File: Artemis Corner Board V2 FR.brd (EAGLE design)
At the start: 132.4 x 63.1 mm, 62 parts, among them U1 TPS562219, U10 TPS562219, U21 LM1085IS, U3 TPS562219, U4 MCP2562FD

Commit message: Everything done exept for scary LEDs
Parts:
- removed C21: 0.1uF, adafruit:C0805
- removed C24, C25, C26: 22uF, adafruit:C0805
- removed L3: 4.7uH, FormE:SRP6540
- removed LED7: GREEN, FormE:CHIPLED_0805
- removed R24: 5.76K, adafruit:R0805
- removed R25, R26: 10K, adafruit:R0805
- removed R27: 1K, adafruit:R0805
- removed U10: TPS562219, FormE:TPS562219
- C12: value 0.1uF -> 8200pF
- C13: value 10uF -> 0.1uF
- C14: value 10uF -> 22uF
- C15: value 8200pF -> 22uF
- C16: value 0.1uF -> 22uF
- C17, C19, C20: value 22uF -> 0.1uF; device adafruit:C0805 -> rcl:C0805
- C18: value 8200pF -> 0.1uF; device adafruit:C0805 -> rcl:C0805
- R5: value 26.1K -> 33.2K
- moved H1 155.9 mm to (9.17, 1.43)
- moved LED1 129.6 mm to (-56.5, 27.3)
- moved R8 97.1 mm to (53.3, 13.3)
- moved R9 97.1 mm to (60.3, -6.35)
- moved C11 96.7 mm to (64.1, 8.89)
- moved U3 96.7 mm to (53.3, 8.89)
- moved C10 96.7 mm to (61.6, 8.89)
- moved C9 96.7 mm to (59.1, 8.89)
- moved R5 96.7 mm to (47.6, 10.8)
- moved R6 96.7 mm to (47.6, 6.35)
- moved C16 83.9 mm to (57.8, 1.27), turned to 0 degrees
- moved L2 83.3 mm to (50.8, -1.91)
- moved LED3 83.0 mm to (55.9, -6.35)
- moved C12 82.2 mm to (50.2, 12.7), turned to 90 degrees
- moved C15 75.7 mm to (57.8, -1.27), turned to 0 degrees
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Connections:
- removed net +1V2: C17.1, C19.1, C20.1, C23.1, L2.P$2, LED3.A, R24.2, U2.11, U2.2, U2.26, U2.42, U2.54, U4.5
- removed net +2V8: C24.1, C25.1, C26.1, L3.P$2, LED7.A, R5.2
- removed net N$1001: R26.2, U10.7
- removed net N$28: LED3.C, R27.2
- removed net SS_5V: C15.1, U10.5
- removed net SW_5V: C16.2, L2.P$1, U10.2
- removed net VBST_5V: C16.1, U10.8
- removed net VFB_5V: R24.1, R25.2, U10.6
- new net IR_SENSOR_1_ANALOG_OUT: H1.28, U2.61
- new net IR_SENSOR_1_DIGITAL_IN: H1.12, U2.45
- new net IR_SENSOR_1_DIGITAL_OUT: H1.15, U2.49
- new net IR_SENSOR_2_ANALOG_OUT: H1.27, U2.62
- new net IR_SENSOR_2_DIGITAL_IN: H1.11, U2.50
- new net IR_SENSOR_2_DIGITAL_OUT: H1.14, U2.48
- new net IR_SENSOR_3_ANALOG_OUT: H1.26, U2.63
- new net IR_SENSOR_3_DIGITAL_IN: H1.10, U2.51
- new net IR_SENSOR_3_DIGITAL_OUT: H1.13, U2.47
- net +12V: now also H1.2, H1.3, H1.4, H1.5, H1.6; no longer H1.21, H1.28
- net +3V3: now also C17.1, C18.1, C19.1, C20.1, C23.1, U2.11, U2.2, U2.26, U2.42, U2.54, U4.5; no longer H1.7, H1.8
- net +5V: now also C14.1, C15.1, C16.1, L2.P$2, LED3.A, R5.2
- net DAMPER_POS_OUT: now also H1.25; no longer H1.35
- net GND: now also C16.2, H1.17, H1.18, H1.19, H1.20; no longer C13.2, C24.2, C25.2, C26.2, H1.2, H1.3, H1.4, H1.5, H1.6, R25.1, R27.1, U10.1
- net N$3: now also LED3.C; no longer LED7.C
- net PROGRAMMING_CAN_N: now also H1.35; no longer H1.34
- net PROGRAMMING_CAN_P: now also H1.34; no longer H1.33
- net SS_5V2: now also C12.1; no longer C18.1
- net STRAIN_GADGE_VOLTMETER_IN_0: no longer U2.8
- net STRAIN_GAUGE_VOLTMETER_OUT: no longer U2.28
- net SW_5V2: now also C13.2, L2.P$1; no longer C21.2, L3.P$1
- net VBST_5V2: now also C13.1; no longer C21.1
- net VCC: no longer C12.1, C13.1, C14.1, R26.1, U10.3
- net WHEEL_SPEED_OUT: now also H1.24; no longer H1.22
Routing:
- net PROGRAMMING_CAN_RX: track 17.2 -> 36.4 mm
- net +3V3: track 1.54 -> 19.8 mm, vias 6 -> 11
- net PROGRAMMING_CAN_TX: track 11.3 -> 26.1 mm
- net +1V2: track 11.0 -> 0.00 mm, vias 4 -> 0
- net N$1001: track 7.73 -> 0.00 mm, vias 2 -> 0
- net VFB_5V: track 6.85 -> 0.00 mm
- net N$11: track 0.00 -> 3.66 mm
- net VBST_5V: track 3.07 -> 0.00 mm
- net SS_5V: track 2.66 -> 0.00 mm
- net +5V: track 3.04 -> 5.48 mm, vias 7 -> 8
- net VCC: track 8.44 -> 6.05 mm, vias 24 -> 18
- net N$28: track 1.76 -> 0.00 mm
- net SW_5V2: track 1.75 -> 0.00 mm, vias 6 -> 8
- net +2V8: track 1.54 -> 0.00 mm, vias 6 -> 0
- net +12V: track 0.00 -> 1.49 mm, vias 7 -> 11
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- added copper zone on layer 15, net +3V3
- added copper zone on layer 15, net +5V
- added copper zone on layer 15, net N$5
- removed copper zone on layer 1, net +2V8
- removed copper zone on layer 1, net SW_5V
- removed copper zone on layer 16, net SW_5V

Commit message: Done  (1st)
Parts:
- added C21: 0.1uF, rcl:C0805
- added LED10, LED11, LED12, LED13, LED14, LED15, LED16, LED17, LED18, LED7, LED8, LED9: APA102C, FormE:5050_LED
- U2: value (none) -> TM4C1231C3PM
- moved LED4 102.7 mm to (29.8, -36.8)
- moved C20 87.8 mm to (8.89, -16.5)
- moved LED2 85.8 mm to (29.8, -22.9), turned to 270 degrees
- moved LED1 80.7 mm to (14.0, -12.1)
- moved C19 79.4 mm to (-6.99, -6.35), turned to 180 degrees
- moved C18 64.7 mm to (-2.54, -27.3)
- moved R10 13.9 mm to (-15.9, 1.91), turned to 90 degrees
- moved C17 1.91 mm to (-16.5, -16.5)
- moved C27 1.91 mm to (-16.5, -14.0)
- moved U2 1.27 mm to (-5.08, -17.1)
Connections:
- removed net N$17: LED1.1
- removed net N$18: LED1.2
- removed net STRAIN_GAUGE_VOLTMETER_OUT: H1.29
- new net N$12: LED4.5, LED7.2
- new net N$13: LED4.6, LED7.1
- new net N$14: LED10.6, LED11.1
- new net N$19: LED11.6, LED12.1
- new net N$20: LED11.5, LED12.2
- new net N$21: LED10.5, LED11.2
- new net N$22: LED10.1, LED9.6
- new net N$23: LED10.2, LED9.5
- new net N$24: LED13.6, LED14.1
- new net N$25: LED14.6, LED15.1
- new net N$26: LED14.5, LED15.2
- new net N$27: LED13.5, LED14.2
- new net N$28: LED12.6, LED13.1
- new net N$29: LED12.5, LED13.2
- new net N$30: LED16.6, LED17.1
- new net N$31: LED17.6, LED18.1
- new net N$32: LED17.5, LED18.2
- new net N$33: LED16.5, LED17.2
- new net N$34: LED15.5, LED16.2
- new net N$35: LED15.6, LED16.1
- new net N$5: LED7.6, LED8.1
- new net N$6: LED8.6, LED9.1
- new net N$7: LED8.5, LED9.2
- new net N$8: LED7.5, LED8.2
- net +3V3: now also C21.1
- net +5V: now also LED10.4, LED11.4, LED12.4, LED13.4, LED14.4, LED15.4, LED16.4, LED17.4, LED18.4, LED7.4, LED8.4, LED9.4
- net GND: now also C21.2, H1.21, H1.22, H1.23, LED10.3, LED11.3, LED12.3, LED13.3, LED14.3, LED15.3, LED16.3, LED17.3, LED18.3, LED7.3, LED8.3, LED9.3; no longer H1.17, H1.18, H1.19
- net IR_SENSOR_1_ANALOG_OUT: now also H1.30; no longer H1.28
- net IR_SENSOR_1_DIGITAL_IN: now also H1.19, U2.52; no longer H1.12, U2.45
- net IR_SENSOR_2_ANALOG_OUT: now also H1.29; no longer H1.27
- net IR_SENSOR_2_DIGITAL_IN: now also H1.18, U2.51; no longer H1.11, U2.50
- net IR_SENSOR_3_ANALOG_OUT: now also H1.28; no longer H1.26
- net IR_SENSOR_3_DIGITAL_IN: now also H1.17, U2.50; no longer H1.10, U2.51
- net SPI_SCARY_LED_CLOCK: now also LED1.2
- net SPI_SCARY_LED_TRANSMIT: now also LED1.1
- net STRAIN_GADGE_VOLTMETER_IN_0: now also H1.27; no longer H1.31
- net STRAIN_GADGE_VOLTMETER_IN_1: now also H1.26; no longer H1.30
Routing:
- net +5V: track 5.48 -> 48.6 mm, vias 8 -> 24
- net GND: track 30.3 -> 70.5 mm, vias 55 -> 71
- net N$24: track 0.00 -> 38.9 mm
- net N$27: track 0.00 -> 38.1 mm
- net SPI_SCARY_LED_CLOCK: track 0.00 -> 37.1 mm, vias 0 -> 2
- net IR_SENSOR_3_DIGITAL_OUT: track 0.00 -> 32.7 mm, vias 0 -> 1
- net IR_SENSOR_2_DIGITAL_IN: track 0.00 -> 32.3 mm, vias 0 -> 1
- net IR_SENSOR_1_DIGITAL_IN: track 0.00 -> 32.0 mm, vias 0 -> 1
- net IR_SENSOR_2_DIGITAL_OUT: track 0.00 -> 32.0 mm, vias 0 -> 1
- net IR_SENSOR_3_DIGITAL_IN: track 0.00 -> 30.1 mm, vias 0 -> 1
- net N$19: track 0.00 -> 28.1 mm
- net N$20: track 0.00 -> 27.5 mm
- net IR_SENSOR_1_DIGITAL_OUT: track 0.00 -> 27.1 mm, vias 0 -> 1
- net N$1: track 0.00 -> 26.8 mm, vias 0 -> 2
- net N$16: track 0.00 -> 23.8 mm, vias 0 -> 2
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- added copper zone on layer 15, net VCC
- removed copper zone on layer 15, net N$5

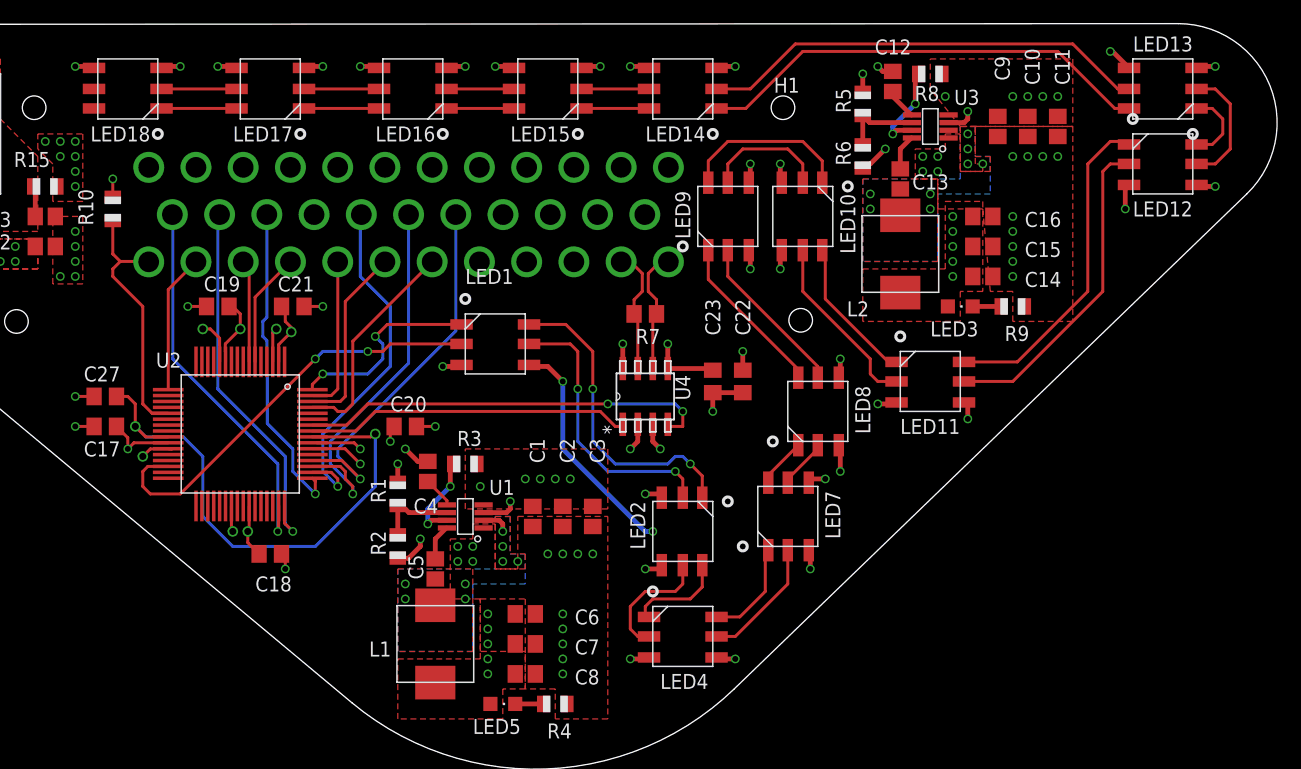
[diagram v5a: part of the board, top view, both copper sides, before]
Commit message: Down to only 4 LEDs
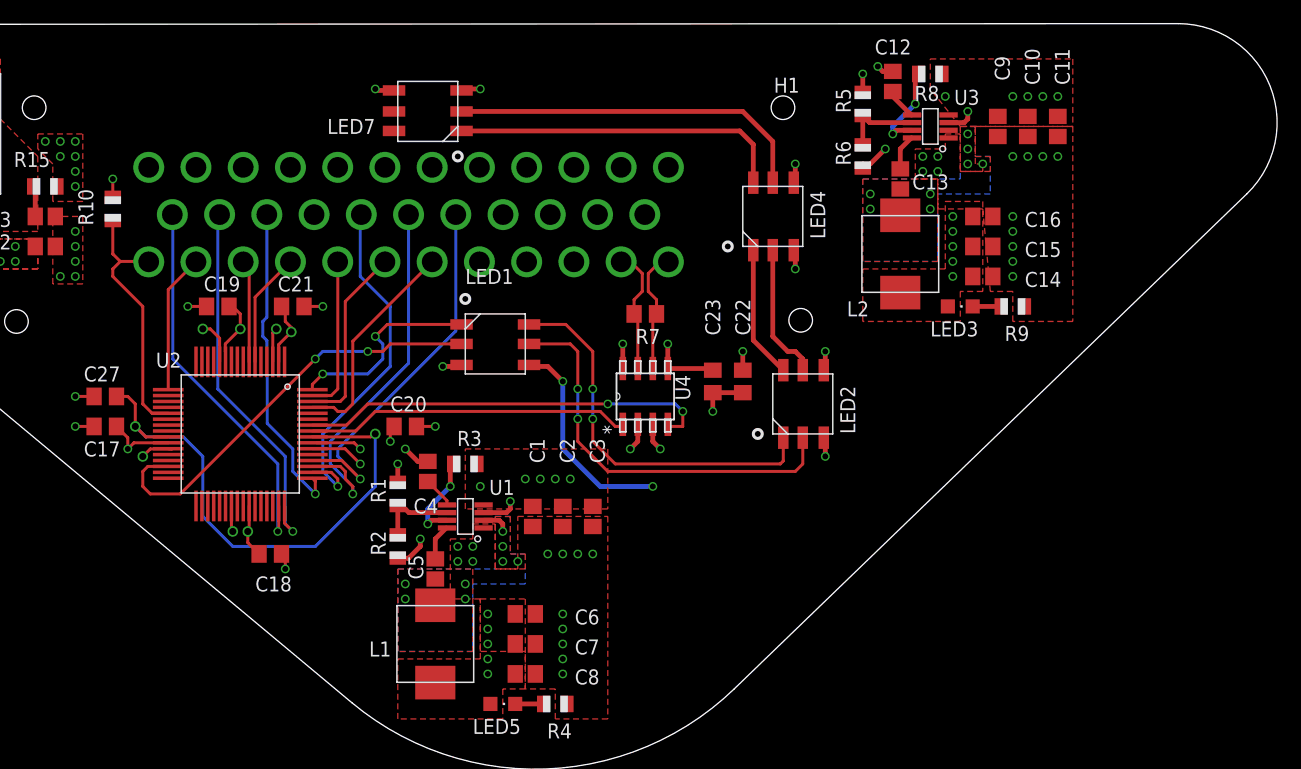
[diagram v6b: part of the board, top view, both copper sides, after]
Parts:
- removed LED10, LED11, LED12, LED13, LED14, LED15, LED16, LED17, LED18, LED8, LED9: APA102C, FormE:5050_LED
- moved LED7 49.8 mm to (13.3, 12.7), turned to 180 degrees
- moved LED4 37.8 mm to (42.5, -1.27), turned to 90 degrees
- moved LED2 16.3 mm to (45.1, -17.1), turned to 90 degrees
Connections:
- removed net N$14: LED10.6, LED11.1
- removed net N$19: LED11.6, LED12.1
- removed net N$20: LED11.5, LED12.2
- removed net N$21: LED10.5, LED11.2
- removed net N$22: LED10.1, LED9.6
- removed net N$23: LED10.2, LED9.5
- removed net N$24: LED13.6, LED14.1
- removed net N$25: LED14.6, LED15.1
- removed net N$26: LED14.5, LED15.2
- removed net N$27: LED13.5, LED14.2
- removed net N$28: LED12.6, LED13.1
- removed net N$29: LED12.5, LED13.2
- removed net N$30: LED16.6, LED17.1
- removed net N$31: LED17.6, LED18.1
- removed net N$32: LED17.5, LED18.2
- removed net N$33: LED16.5, LED17.2
- removed net N$34: LED15.5, LED16.2
- removed net N$35: LED15.6, LED16.1
- removed net N$5: LED7.6, LED8.1
- removed net N$6: LED8.6, LED9.1
- removed net N$7: LED8.5, LED9.2
- removed net N$8: LED7.5, LED8.2
- net +5V: no longer LED10.4, LED11.4, LED12.4, LED13.4, LED14.4, LED15.4, LED16.4, LED17.4, LED18.4, LED8.4, LED9.4
- net GND: no longer LED10.3, LED11.3, LED12.3, LED13.3, LED14.3, LED15.3, LED16.3, LED17.3, LED18.3, LED8.3, LED9.3
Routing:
- net N$24: track 38.9 -> 0.00 mm
- net N$27: track 38.1 -> 0.00 mm
- net N$19: track 28.1 -> 0.00 mm
- net N$20: track 27.5 -> 0.00 mm
- net N$12: track 10.7 -> 30.9 mm
- net +5V: track 48.6 -> 28.5 mm, vias 24 -> 13
- net N$13: track 8.62 -> 28.4 mm
- net GND: track 70.5 -> 51.4 mm, vias 71 -> 60
- net N$21: track 16.3 -> 0.00 mm
- net N$22: track 14.7 -> 0.00 mm
- net N$6: track 14.0 -> 0.00 mm
- net N$7: track 14.0 -> 0.00 mm
- net N$14: track 12.5 -> 0.00 mm
- net N$16: track 23.8 -> 34.6 mm
- net N$29: track 10.6 -> 0.00 mm
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
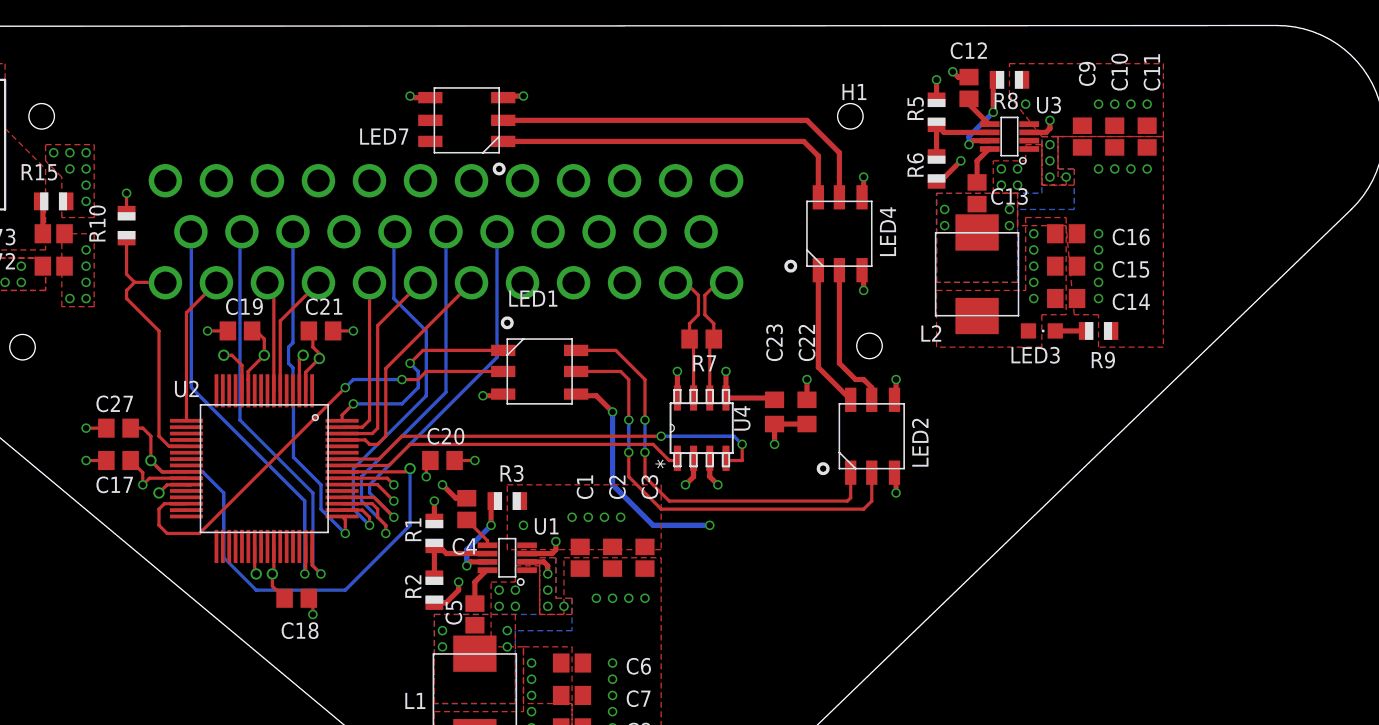
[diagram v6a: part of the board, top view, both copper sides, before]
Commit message: Added decoupling CAPS and Button for reset
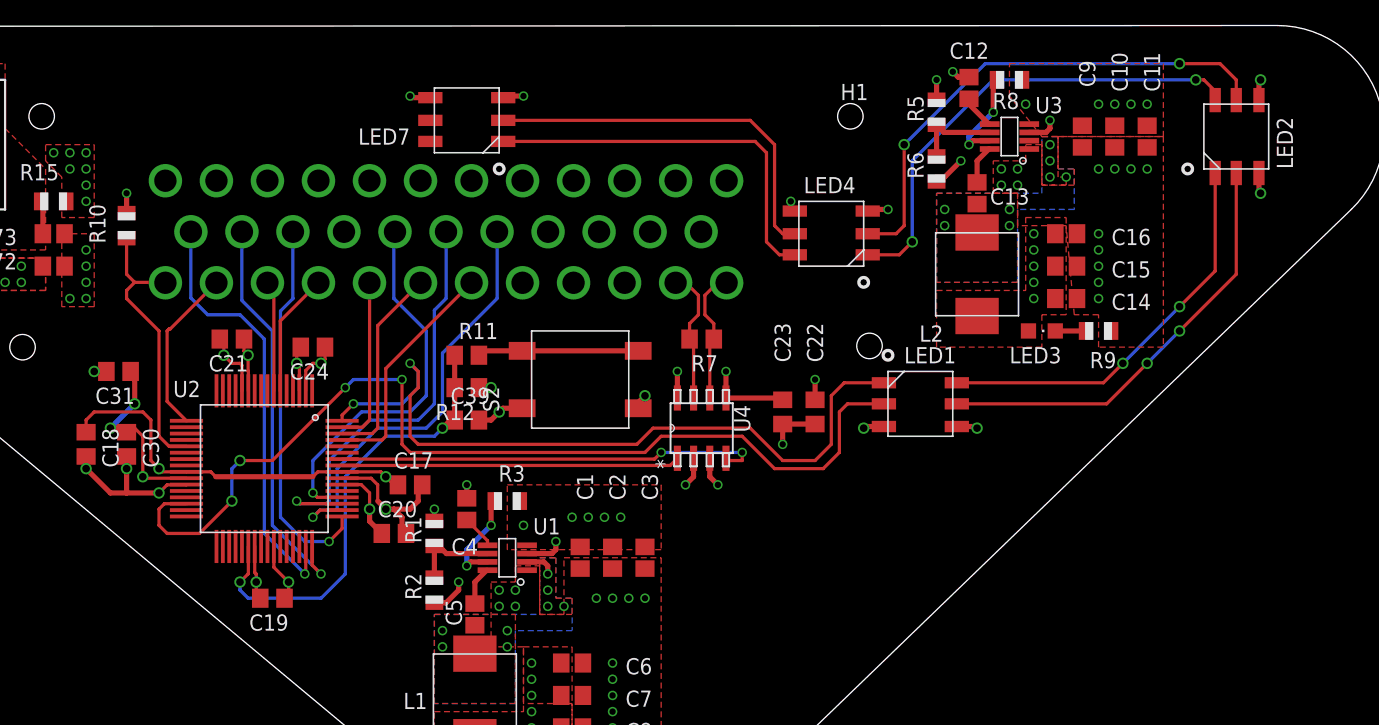
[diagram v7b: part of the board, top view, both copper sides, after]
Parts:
- removed C27: 3.3uF, rcl:C0805
- added C24, C30: 0.1uF, rcl:C0805
- added C31: 20uF, rcl:C0805
- added C39: 1uF, rcl:C0805
- added R11: 100, rcl:R0805
- added R12: 2.2K, rcl:R0805
- added S2: TE-FSM4JSMATR, FormE:TE-FSM4JSMATR
- C18: value 0.1uF -> 3.3uF
- moved LED2 37.0 mm to (73.7, 6.35)
- moved LED1 30.0 mm to (43.8, -14.6)
- moved C17 22.9 mm to (6.35, -18.4), turned to 0 degrees
- moved C19 21.1 mm to (-4.45, -27.3)
- moved C18 20.4 mm to (-19.1, -15.2), turned to 270 degrees
- moved C21 7.01 mm to (-7.62, -6.99), turned to 180 degrees
- moved C20 6.87 mm to (5.08, -22.2)
- moved LED4 5.12 mm to (41.9, 3.81), turned to 180 degrees
- moved C23 0.64 mm to (35.6, -12.7)
- moved C22 0.63 mm to (38.1, -12.7)
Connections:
- new net MCU_RESET: C39.1, R11.1, R12.2, U2.38
- new net N$18: R11.2, S2.1, S2.2
- net +3V3: now also C24.1, C30.1, C31.1, R12.1; no longer C17.1, C18.1
- net GND: now also C24.2, C30.2, C31.2, C39.2, S2.3, S2.4; no longer C27.2
- net IR_SENSOR_1_DIGITAL_IN: now also U2.50; no longer U2.52
- net IR_SENSOR_3_DIGITAL_IN: now also U2.52; no longer U2.50
- net P$40: now also C17.1, C18.1; no longer C27.1
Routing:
- net SPI_SCARY_LED_TRANSMIT: track 17.2 -> 59.5 mm
- net SPI_SCARY_LED_CLOCK: track 37.1 -> 78.1 mm, vias 2 -> 4
- net MCU_RESET: track 0.00 -> 36.1 mm, vias 0 -> 2
- net N$15: track 11.6 -> 40.2 mm, vias 0 -> 2
- net N$10: track 11.2 -> 37.7 mm, vias 0 -> 2
- net +5V: track 28.5 -> 11.5 mm, vias 13 -> 12
- net GND: track 51.4 -> 68.3 mm, vias 60 -> 59
- net P$40: track 46.4 -> 30.2 mm
- net N$18: track 0.00 -> 12.6 mm
- net +3V3: track 35.5 -> 44.6 mm, vias 13 -> 15
- net IR_SENSOR_1_DIGITAL_OUT: track 27.1 -> 29.8 mm
- net N$13: track 28.4 -> 30.6 mm
- net IR_SENSOR_1_DIGITAL_IN: track 32.0 -> 33.9 mm
- net IR_SENSOR_3_DIGITAL_OUT: track 32.7 -> 34.2 mm
- net PROGRAMMING_CAN_RX: track 35.0 -> 33.6 mm
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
